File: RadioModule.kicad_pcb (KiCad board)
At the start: 4 copper layers, 16 x 18 mm, 43 parts, among them J1 Conn_01x01_Pin, J10 Conn_01x01_Pin, J11 Conn_01x01_Pin, J12 Conn_01x01_Pin, J13 Conn_01x01_Pin, J14 Conn_01x01_Pin, J15 Conn_01x01_Pin, J16 Conn_01x01_Pin, J2 Conn_01x01_Pin, J3 Conn_01x01_Pin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

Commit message: Final Commit V1.0
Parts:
- removed the ? at (93.9, 86.2)
- removed the ? at (101.9, 86.2)
- added ?: , , F.Cu at (101.9, 86.0)
- added ?: , , F.Cu at (93.9, 86.0)
- moved ? 0.45 mm to (101.6, 70.2)
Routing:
- net NRST: track 18.4 -> 17.8 mm
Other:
- board size 16 x 18 mm -> 16 x 17.2 mm

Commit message: Moved a via
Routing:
- net 3V3: track 4.88 -> 5.89 mm

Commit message: Crystal Caps sized
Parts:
- C3, C4: value 1nF -> 4pF
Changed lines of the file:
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@@
         (effects (font (size 1 1) (thickness 0.15)))
     )
-    (fp_text value "1nF" (at 0 1.16) (layer "F.Fab")
+    (fp_text value "4pF" (at 0 1.16) (layer "F.Fab")
         (effects (font (size 1 1) (thickness 0.15)))
     )
@@
         (effects (font (size 1 1) (thickness 0.15)))
     )
-    (fp_text value "1nF" (at 0 1.16) (layer "F.Fab") hide
+    (fp_text value "4pF" (at 0 1.16) (layer "F.Fab") hide
         (effects (font (size 1 1) (thickness 0.15)))
     )

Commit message: commit
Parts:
- added G***: LOGO, LOGO, F.Cu at (109.6, 74.6)
- added G***: LOGO, LOGO, F.Cu at (86.4, 81.5)
- added G***: LOGO, LOGO, F.Cu at (86.4, 72.5)
- added G***: LOGO, LOGO, F.Cu at (109.6, 83.6)
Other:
- board size 16 x 17.2 mm -> 28.4 x 17.2 mm

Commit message: Put silkscreen on the back too
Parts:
- added G***: LOGO, LOGO, B.Cu at (109.7, 81.2)
- added G***: LOGO, LOGO, B.Cu at (86.5, 83.7)
- added G***: LOGO, LOGO, B.Cu at (109.7, 72.2)
- added G***: LOGO, LOGO, B.Cu at (86.5, 74.7)

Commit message: actual final commit hopefully
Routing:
- net GND: vias 18 -> 38
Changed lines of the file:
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@@
   (segment (start 97.2415 75.422999) (end 98.4685 76.649999) (width 0.3) (layer "F.Cu") (net 3))
   (segment (start 98.418501 77.1) (end 98.4685 77.149999) (width 0.3) (layer "F.Cu") (net 3))
+  (via (at 91.47 72.03) (size 0.45) (drill 0.25) (layers "F.Cu" "B.Cu") (free) (net 3))
   (via (at 98.4685 77.149999) (size 0.5) (drill 0.3) (layers "F.Cu" "B.Cu") (net 3))
+  (via (at 103.56 86.02) (size 0.45) (drill 0.25) (layers "F.Cu" "B.Cu") (free) (net 3))
   (via (at 96.78 70.35) (size 0.5) (drill 0.3) (layers "F.Cu" "B.Cu") (free) (net 3))
   (via (at 92.38 70.15) (size 0.5) (drill 0.3) (layers "F.Cu" "B.Cu") (free) (net 3))
+  (via (at 93.91 73.84) (size 0.45) (drill 0.25) (layers "F.Cu" "B.Cu") (free) (net 3))
+  (via (at 104.32 70.26) (size 0.5) (drill 0.3) (layers "F.Cu" "B.Cu") (free) (net 3))
+  (via (at 99.58 74.37) (size 0.45) (drill 0.25) (layers "F.Cu" "B.Cu") (free) (net 3))
   (via (at 92.13 73.19) (size 0.5) (drill 0.3) (layers "F.Cu" "B.Cu") (free) (net 3))
-  (via (at 97.98 70.85) (size 0.5) (drill 0.3) (layers "F.Cu" "B.Cu") (free) (net 3))
+  (via (at 95.05 77.59) (size 0.45) (drill 0.25) (layers "F.Cu" "B.Cu") (free) (net 3))
+  (via (at 99.49 70.28) (size 0.5) (drill 0.3) (layers "F.Cu" "B.Cu") (free) (net 3))
+  (via (at 100.36 86.06) (size 0.45) (drill 0.25) (layers "F.Cu" "B.Cu") (free) (net 3))
   (via (at 102.88 78.747878) (size 0.5) (drill 0.3) (layers "F.Cu" "B.Cu") (net 3))
   (via (at 93.24 74.19) (size 0.5) (drill 0.3) (layers "F.Cu" "B.Cu") (free) (net 3))
   (via (at 94.25 73.3) (size 0.5) (drill 0.3) (layers "F.Cu" "B.Cu") (free) (net 3))
   (via (at 96.71 72) (size 0.5) (drill 0.3) (layers "F.Cu" "B.Cu") (free) (net 3))
+  (via (at 92.48 81.06) (size 0.45) (drill 0.25) (layers "F.Cu" "B.Cu") (free) (net 3))
   (via (at 93.5 70.15) (size 0.5) (drill 0.3) (layers "F.Cu" "B.Cu") (free) (net 3))
   (via (at 93.24 80.66) (size 0.5) (drill 0.3) (layers "F.Cu" "B.Cu") (free) (net 3))
   (via (at 95.84 73.13) (size 0.5) (drill 0.3) (layers "F.Cu" "B.Cu") (free) (net 3))
-  (via (at 98.78 71.85) (size 0.5) (drill 0.3) (layers "F.Cu" "B.Cu") (free) (net 3))
+  (via (at 93.98 72.52) (size 0.45) (drill 0.25) (layers "F.Cu" "B.Cu") (free) (net 3))
+  (via (at 98.27 71.23) (size 0.5) (drill 0.3) (layers "F.Cu" "B.Cu") (free) (net 3))
+  (via (at 104.25 72.15) (size 0.5) (drill 0.3) (layers "F.Cu" "B.Cu") (free) (net 3))
   (via (at 94.16 77.95) (size 0.5) (drill 0.3) (layers "F.Cu" "B.Cu") (free) (net 3))
+  (via (at 104.72 85.01) (size 0.45) (drill 0.25) (layers "F.Cu" "B.Cu") (free) (net 3))
+  (via (at 98.7 84.99) (size 0.45) (drill 0.25) (layers "F.Cu" "B.Cu") (free) (net 3))
   (via (at 95.78 70.15) (size 0.5) (drill 0.3) (layers "F.Cu" "B.Cu") (free) (net 3))
-  (via (at 92.13 72.13) (size 0.5) (drill 0.3) (layers "F.Cu" "B.Cu") (free) (net 3))
+  (via (at 95.07 73.13) (size 0.45) (drill 0.25) (layers "F.Cu" "B.Cu") (free) (net 3))
+  (via (at 93.2 83.71) (size 0.45) (drill 0.25) (layers "F.Cu" "B.Cu") (free) (net 3))
+  (via (at 92.41 73.95) (size 0.45) (drill 0.25) (layers "F.Cu" "B.Cu") (free) (net 3))
+  (via (at 92.45 77.63) (size 0.45) (drill 0.25) (layers "F.Cu" "B.Cu") (free) (net 3))
+  (via (at 98.71 71.9) (size 0.45) (drill 0.25) (layers "F.Cu" "B.Cu") (free) (net 3))
+  (via (at 92.2 72.38) (size 0.5) (drill 0.3) (layers "F.Cu" "B.Cu") (free) (net 3))
+  (via (at 91.44 70.02) (size 0.45) (drill 0.25) (layers "F.Cu" "B.Cu") (free) (net 3))
+  (via (at 95.42 86.06) (size 0.45) (drill 0.25) (layers "F.Cu" "B.Cu") (free) (net 3))
   (via (at 95.63 82.2) (size 0.5) (drill 0.3) (layers "F.Cu" "B.Cu") (free) (net 3))
+  (via (at 91.86 86.09) (size 0.45) (drill 0.25) (layers "F.Cu" "B.Cu") (free) (net 3))
   (via (at 94.64 70.15) (size 0.5) (drill 0.3) (layers "F.Cu" "B.Cu") (free) (net 3))
   (segment (start 93.587818 82.91) (end 95.827 82.91) (width 0.2) (layer "F.Cu") (net 4))

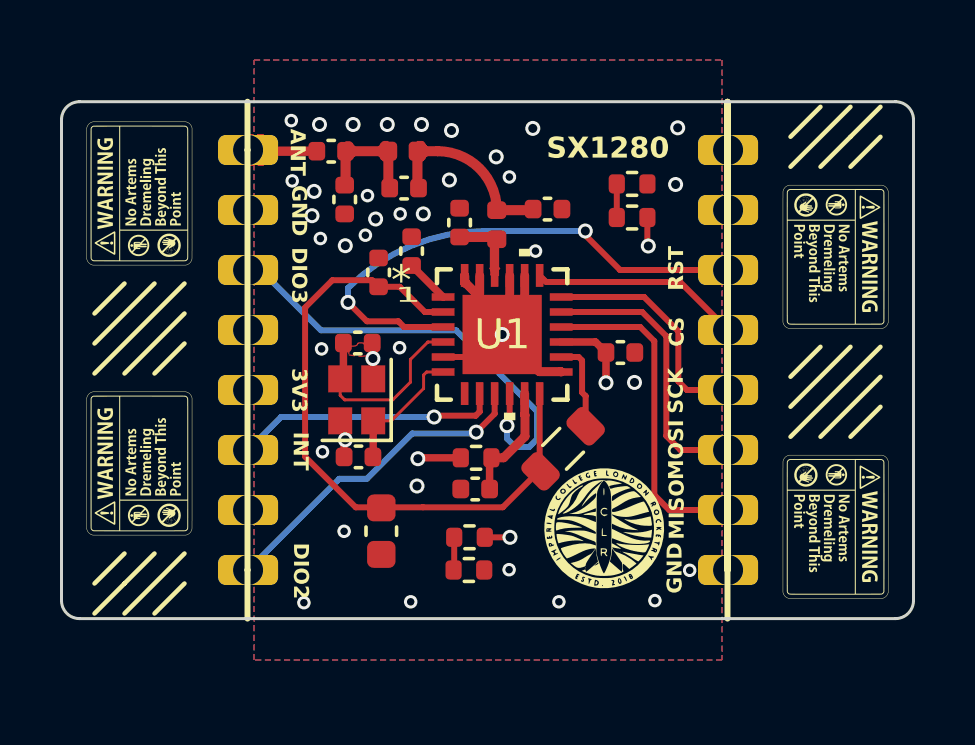
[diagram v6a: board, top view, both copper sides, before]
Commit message: radio module ordering
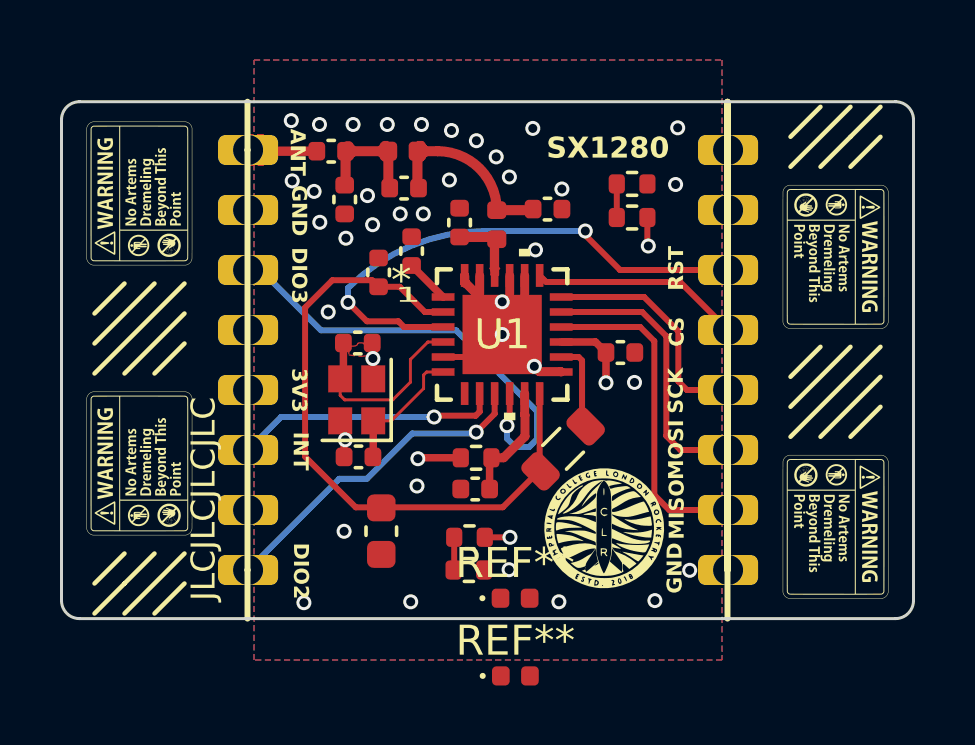
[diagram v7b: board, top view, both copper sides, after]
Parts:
- added REF**: LED_0402_1005Metric, LED_SMD:LED_0402_1005Metric, F.Cu at (98.9, 88.5)
- added REF**: LED_0402_1005Metric, LED_SMD:LED_0402_1005Metric, F.Cu at (98.9, 85.9)
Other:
- board text added: "JLCJLCJLCJLC"
